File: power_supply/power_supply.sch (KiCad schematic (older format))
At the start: 36 parts, among them J1 Conn_01x04_Male, J2 Conn_01x03_Male, J3 Conn_01x03_Male, J4 Conn_01x03_Male, U1 LM7815_TO220, U2 LM7915_TO220, U3 LM7805_TO220

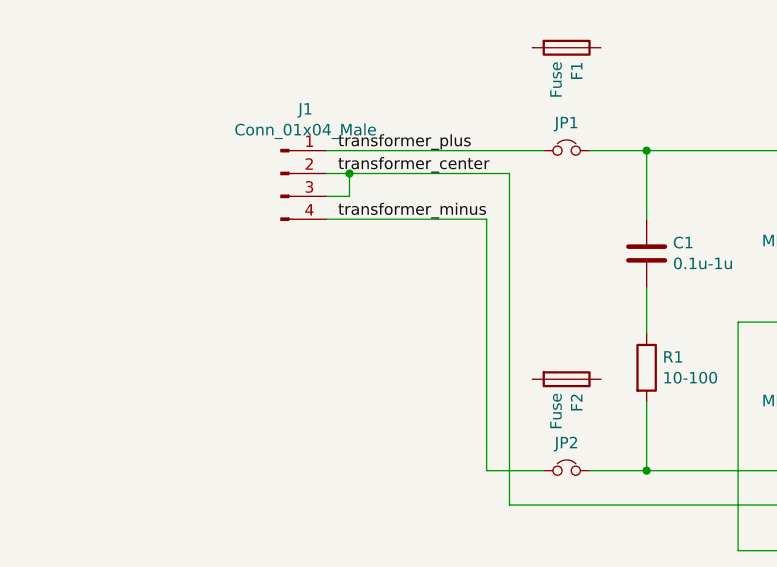
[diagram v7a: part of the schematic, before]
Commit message: add note clarifying input connector AWG & voltage/current limits
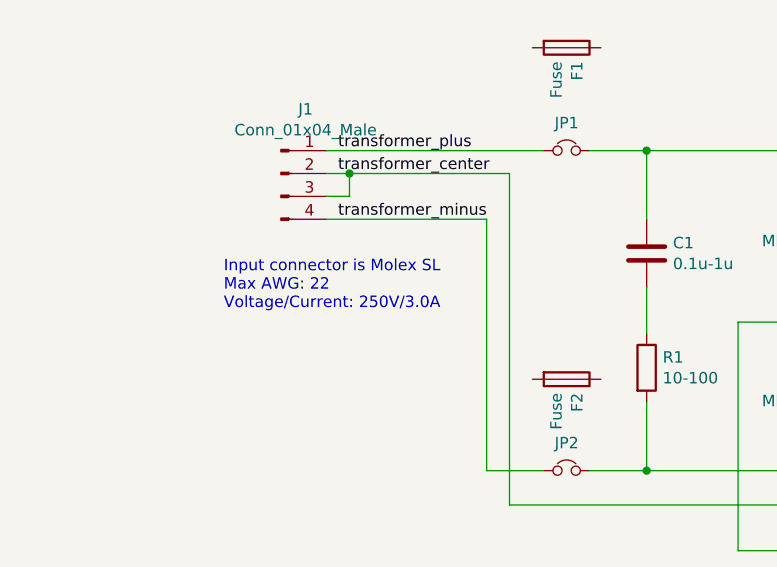
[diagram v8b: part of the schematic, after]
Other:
- note added: "Input connector is Molex SL\nMax AWG: 22\nVoltage/Current: 250V/3.0A"
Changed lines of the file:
@@
 Wire Wire Line
 	1200 1350 1900 1350
+Text Notes 650  1950 0    50   ~ 0
+Input connector is Molex SL\nMax AWG: 22\nVoltage/Current: 250V/3.0A
 $EndSCHEMATC
